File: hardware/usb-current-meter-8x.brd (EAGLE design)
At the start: 78.5 x 29.2 mm, 39 parts, among them IC3 MEGA48/88/168-AU, IC9 OPA2234U, X7 MC2

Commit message: hardware: progress save
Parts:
- added C14, C17, C19, C22, C27, C29, C4, C7: 100n, rcl:C0805
- added C15, C16, C18, C20, C21, C23, C25, C26, C28, C5, C6, C8: 1u, rcl:C0805
- added D1, D2, D3, D4: BAT54, diode:SOT23
- added IC2, IC4, IC5, IC6: OPA2234U, burr-brown:SO08
- added R10, R14, R15, R16, R17, R18, R19, R22, R23, R24, R25, R26, R27, R30, R31, R32, R33, R42, R43, R5, R6, R7, R8, R9: tbd, rcl:R0603
- added R11, R20, R28, R36: 100k, rcl:R0603
- added R12, R21, R29, R37, R4: Rload, rcl:R0805
- added X1, X2, X3, X4, X5: MC2, con-phoenix-381_l:MC2
- moved D7 11.0 mm to (45.5, 18.7)
- moved R56 11.0 mm to (37.4, 24.4)
- moved R57 11.0 mm to (37.4, 21.1)
- moved R60 11.0 mm to (37.4, 17.9)
- moved C39 11.0 mm to (38.2, 27.2)
- moved C42 11.0 mm to (43.1, 16.3)
- moved IC9 11.0 mm to (43.1, 19.9)
- moved R53 11.0 mm to (43.1, 26.4)
- moved R54 11.0 mm to (46.7, 26.4)
- moved R55 11.0 mm to (46.7, 21.5)
- moved R58 11.0 mm to (42.3, 21.1)
- moved R59 11.0 mm to (38.2, 25.6)
- moved X7 11.0 mm to (43.1, 24.0)
- moved C40 11.0 mm to (38.6, 20.3)
- moved C41 11.0 mm to (38.6, 22.4)
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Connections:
- net SC_IN_B renamed SC_IN_B_0
- removed net SC_IN_A: R53.2, R54.1, X7.1
- new net N$10: IC2.6, R7.2, R8.1
- new net N$11: IC2.7, R11.1, R8.2
- new net N$12: IC4.2, R14.2, R15.1
- new net N$13: D2.1, IC4.1
- new net N$14: D2.3, IC4.5, R15.2
- new net N$15: IC4.6, R16.2, R17.1
- new net N$16: IC4.7, R17.2, R20.1
- new net N$17: IC6.2, R30.2, R31.1
- new net N$18: D4.1, IC6.1
- new net N$19: D4.3, IC6.5, R31.2
- new net N$20: IC6.6, R32.2, R33.1
- new net N$21: IC6.7, R33.2, R36.1
- new net N$22: IC5.2, R22.2, R23.1
- new net N$23: D3.1, IC5.1
- new net N$24: D3.3, IC5.5, R23.2
- new net N$25: IC5.6, R24.2, R25.1
- new net N$26: IC5.7, R25.2, R28.1
- new net N$7: IC2.2, R5.2, R6.1
- new net N$8: D1.1, IC2.1
- new net N$9: D1.3, IC2.5, R6.2
- new net SC_IN_A_0: R29.2, R30.1, R53.2, R54.1, X4.1, X7.1
- new net SC_IN_A_1: R4.2, R5.1, X1.1
- new net SC_IN_A_2: R12.2, R14.1, X2.1
- new net SC_IN_A_3: R21.2, R22.1, X3.1
- new net SC_IN_B_1: C4.1, R10.2, R4.1, R9.1, X1.2
- new net SC_IN_B_2: C14.1, R12.1, R18.1, R19.2, X2.2
- new net SC_IN_B_3: C19.1, R21.1, R26.1, R27.2, X3.2
- new net SC_IN_B_5: C29.1, R37.1, R42.1, R43.2, X5.2
- net GND: now also C14.2, C15.2, C16.2, C17.2, C18.2, C19.2, C20.2, C21.2, C22.2, C23.2, C25.2, C26.2, C27.2, C28.2, C29.2, C4.2, C5.2, C6.2, C7.2, C8.2, IC2.3, IC2.4, IC4.3, IC4.4, IC5.3, IC5.4, IC6.3, IC6.4, R10.1, R16.1, R19.1, R24.1, R27.1, R29.1, R32.1, R43.1, R7.1, X4.2
- net IN_CH0: now also C25.1, C26.1, C28.1, R36.2
- net IN_CH1: now also C5.1, C6.1, C8.1, R11.2, R37.2, X5.1
- net IN_CH2: now also C15.1, C16.1, C18.1, R20.2
- net IN_CH3: now also C20.1, C21.1, C23.1, R28.2
- net VCC: now also C17.1, C22.1, C27.1, C7.1, IC2.8, IC4.8, IC5.8, IC6.8, R18.2, R26.2, R42.2, R9.2
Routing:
- net VCC: track 64.1 -> 85.3 mm, vias 5 -> 7
- net IN_CH1: track 0.00 -> 10.7 mm, vias 0 -> 1
- net SC_IN_B_2: track 0.00 -> 10.3 mm
- net SC_IN_B_1: track 0.00 -> 10.3 mm
- net SC_IN_B_3: track 0.00 -> 10.3 mm
- net N$7: track 0.00 -> 9.73 mm, vias 0 -> 1
- net N$12: track 0.00 -> 9.73 mm, vias 0 -> 1
- net N$22: track 0.00 -> 9.73 mm, vias 0 -> 1
- net SC_IN_B_5: track 0.00 -> 8.94 mm
- net N$14: track 0.00 -> 8.79 mm, vias 0 -> 1
- net N$24: track 0.00 -> 8.79 mm, vias 0 -> 1
- net IN_CH3: track 0.00 -> 7.69 mm, vias 0 -> 1
- net IN_CH2: track 0.00 -> 7.69 mm, vias 0 -> 1
- net N$9: track 0.00 -> 6.74 mm, vias 0 -> 1
- net SC_IN_A_0: track 0.00 -> 5.89 mm
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
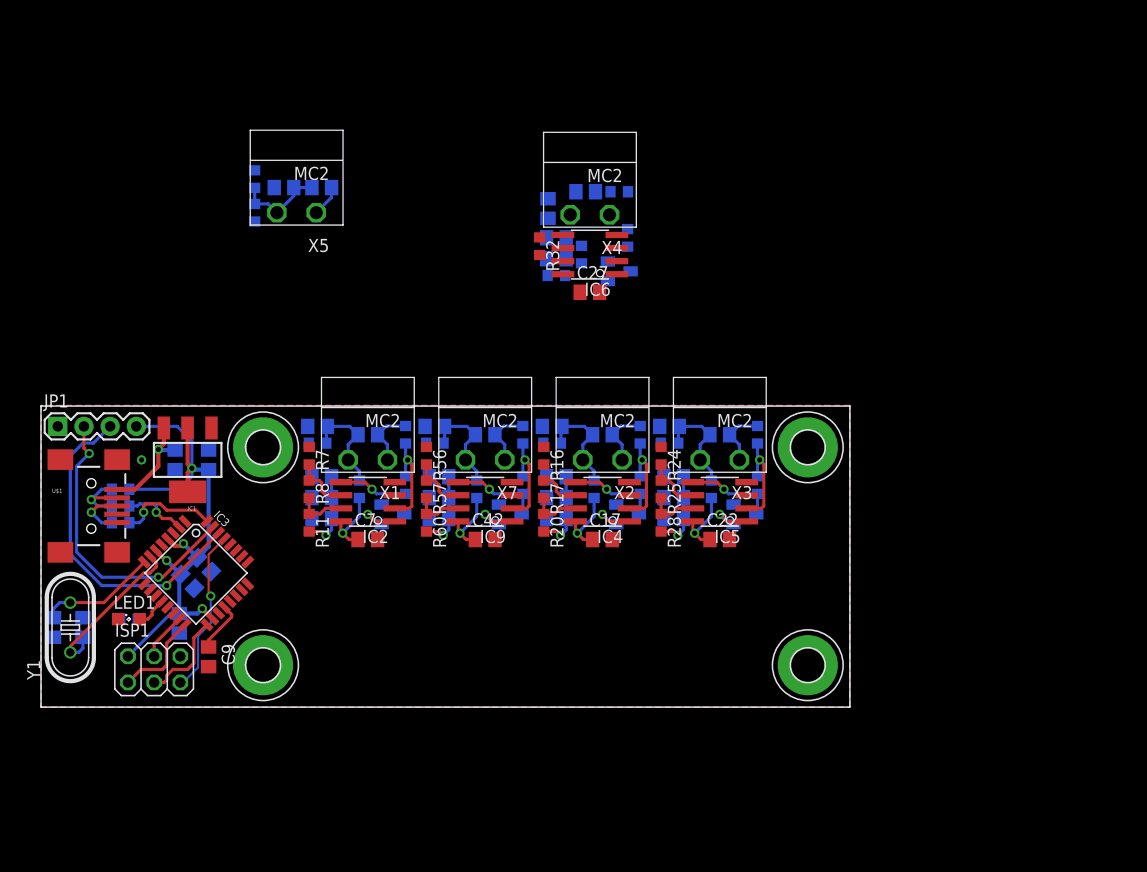
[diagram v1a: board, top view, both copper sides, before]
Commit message: hardware: 8x schematic updated
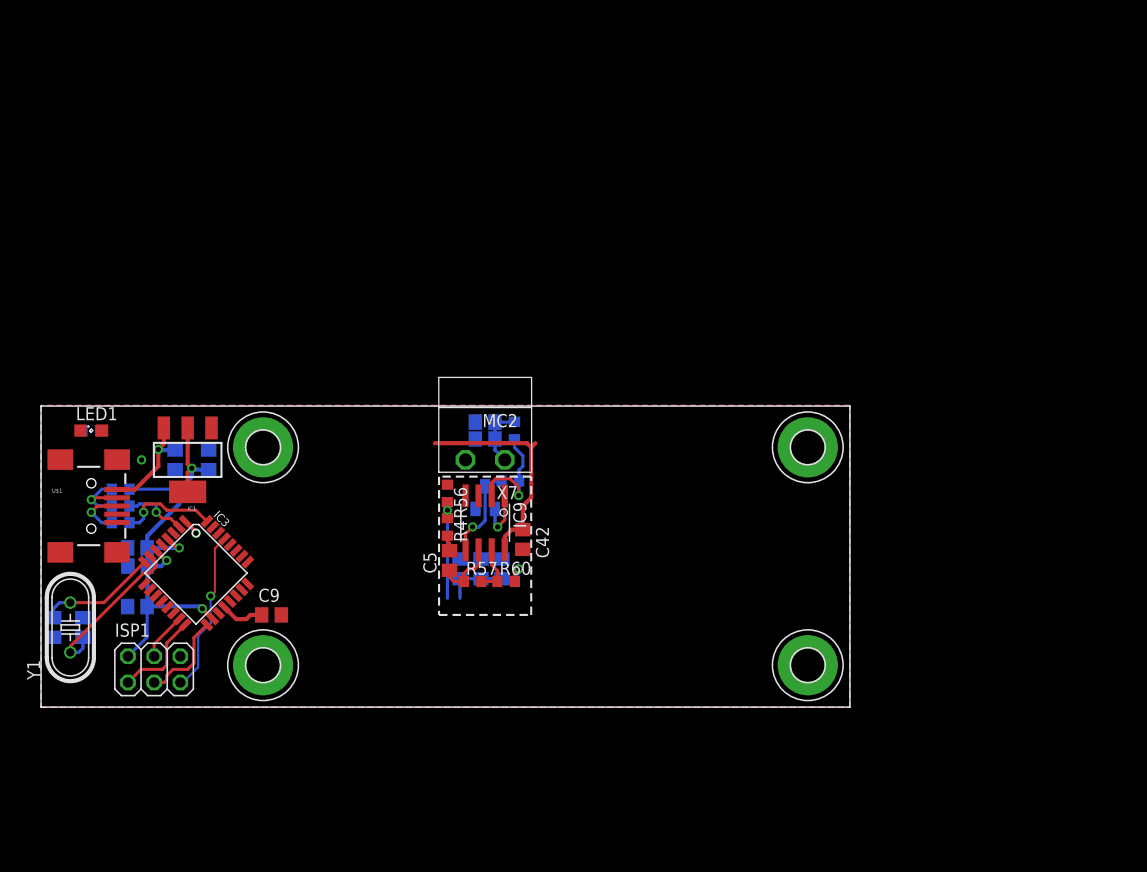
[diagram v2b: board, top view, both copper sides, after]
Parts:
- removed C14, C17, C19, C22, C27, C29, C39, C7: 100n, rcl:C0805
- removed C15, C16, C18, C20, C21, C23, C25, C26, C28, C6, C8: 1u, rcl:C0805
- removed D1, D2, D3, D4: BAT54, diode:SOT23
- removed IC2, IC4, IC5, IC6: OPA2234U, burr-brown:SO08
- removed JP1: (no value), SparkFun:1X04
- removed R10, R14, R15, R16, R17, R18, R19, R22, R23, R24, R25, R26, R27, R30, R31, R32, R33, R42, R43, R5, R58, R59, R6, R7, R8, R9: tbd, rcl:R0603
- removed R11, R20, R28, R36: 100k, rcl:R0603
- removed R12, R21, R29, R37: Rload, rcl:R0805
- removed X1, X2, X3, X4, X5: MC2, con-phoenix-381_l:MC2
- C5: value 1u -> 100n
- R4: value Rload -> tbd; device rcl:R0805 -> rcl:R0603
- moved LED1 18.7 mm to (4.88, 26.8)
- moved R13 18.7 mm to (4.88, 26.8)
- moved C4 16.3 mm to (43.1, 27.6)
- moved C5 13.0 mm to (39.6, 14.2), flipped to the top, turned to 90 degrees
- moved R4 11.8 mm to (39.4, 17.5), flipped to the top, turned to 270 degrees
- moved R57 10.00 mm to (41.9, 12.2), turned to 0 degrees
- moved R60 9.59 mm to (45.1, 12.2), turned to 0 degrees
- moved C41 9.17 mm to (40.6, 13.4), turned to 90 degrees
- moved C40 8.02 mm to (42.7, 13.4), turned to 90 degrees
- moved C43 7.81 mm to (44.7, 13.4), turned to 90 degrees
- moved C9 7.33 mm to (22.4, 8.94), turned to 0 degrees
- moved C13 6.70 mm to (9.35, 15.4), turned to 0 degrees
- moved C3 5.07 mm to (9.37, 13.7), turned to 0 degrees
- moved C12 4.38 mm to (9.35, 9.75), turned to 0 degrees
- moved R56 4.18 mm to (39.4, 20.7)
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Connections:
- net IN_CH4 renamed CH4
- net IN_CH5 renamed CH5
- net IN_CH6 renamed CH6
- net IN_CH7 renamed CH7
- removed net IN_CH0: C25.1, C26.1, C28.1, C40.1, C41.1, C43.1, IC3.23, R36.2, R60.2
- removed net IN_CH1: C5.1, C6.1, C8.1, IC3.24, R11.2, R37.2, X5.1
- removed net IN_CH2: C15.1, C16.1, C18.1, IC3.25, R20.2
- removed net IN_CH3: C20.1, C21.1, C23.1, IC3.26, R28.2
- removed net N$10: IC2.6, R7.2, R8.1
- removed net N$11: IC2.7, R11.1, R8.2
- removed net N$12: IC4.2, R14.2, R15.1
- removed net N$13: D2.1, IC4.1
- removed net N$14: D2.3, IC4.5, R15.2
- removed net N$15: IC4.6, R16.2, R17.1
- removed net N$16: IC4.7, R17.2, R20.1
- removed net N$17: IC6.2, R30.2, R31.1
- removed net N$18: D4.1, IC6.1
- removed net N$19: D4.3, IC6.5, R31.2
- removed net N$20: IC6.6, R32.2, R33.1
- removed net N$21: IC6.7, R33.2, R36.1
- removed net N$22: IC5.2, R22.2, R23.1
- removed net N$23: D3.1, IC5.1
- removed net N$24: D3.3, IC5.5, R23.2
- removed net N$25: IC5.6, R24.2, R25.1
- removed net N$26: IC5.7, R25.2, R28.1
- removed net N$8: D1.1, IC2.1
- removed net N$9: D1.3, IC2.5, R6.2
- removed net SC_IN_A_0: R29.2, R30.1, R53.2, R54.1, X4.1, X7.1
- removed net SC_IN_A_1: R4.2, R5.1, X1.1
- removed net SC_IN_A_2: R12.2, R14.1, X2.1
- removed net SC_IN_A_3: R21.2, R22.1, X3.1
- removed net SC_IN_B_0: C39.1, R53.1, R58.1, R59.2, X7.2
- removed net SC_IN_B_1: C4.1, R10.2, R4.1, R9.1, X1.2
- removed net SC_IN_B_2: C14.1, R12.1, R18.1, R19.2, X2.2
- removed net SC_IN_B_3: C19.1, R21.1, R26.1, R27.2, X3.2
- removed net SC_IN_B_5: C29.1, R37.1, R42.1, R43.2, X5.2
- removed net UART_RX: IC3.30, JP1.3
- removed net UART_TX: IC3.31, JP1.2
- new net CH0: C40.1, C41.1, C43.1, IC3.23, R60.2
- new net CH0_GAIN: IC3.30, R4.1, R56.2
- new net CH0_IN: C4.1, R53.2, R54.1, X7.1
- new net CH1: IC3.24
- new net CH1_GAIN: IC3.31
- new net CH2: IC3.25
- new net CH2_GAIN: IC3.9
- new net CH3: IC3.26
- new net CH3_GAIN: IC3.10
- new net CH4_GAIN: IC3.11
- new net CH5_GAIN: IC3.12
- new net CH6_GAIN: IC3.13
- new net CH7_GAIN: IC3.14
- net GND: now also R53.1, X7.2; no longer C14.2, C15.2, C16.2, C17.2, C18.2, C19.2, C20.2, C21.2, C22.2, C23.2, C25.2, C26.2, C27.2, C28.2, C29.2, C39.2, C5.2, C6.2, C7.2, C8.2, IC2.3, IC2.4, IC4.3, IC4.4, IC5.3, IC5.4, IC6.3, IC6.4, JP1.1, R10.1, R16.1, R19.1, R24.1, R27.1, R29.1, R32.1, R43.1, R59.1, R7.1, X4.2
- net LED: now also IC3.1; no longer IC3.12
- net N$40: now also C5.1; no longer R56.2
- net N$7: now also C5.2, R4.2; no longer IC2.2, R5.2, R6.1
- net VCC: no longer C17.1, C22.1, C27.1, C7.1, IC2.8, IC4.8, IC5.8, IC6.8, JP1.4, R18.2, R26.2, R42.2, R58.2, R9.2
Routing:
- net UART_RX: track 32.4 -> 0.00 mm, vias 1 -> 0
- net UART_TX: track 29.1 -> 0.00 mm, vias 2 -> 0
- net VCC: track 85.3 -> 70.6 mm, vias 7 -> 4
- net IN_CH1: track 10.7 -> 0.00 mm, vias 1 -> 0
- net SC_IN_B_2: track 10.3 -> 0.00 mm
- net SC_IN_B_0: track 10.3 -> 0.00 mm
- net SC_IN_B_1: track 10.3 -> 0.00 mm
- net SC_IN_B_3: track 10.3 -> 0.00 mm
- net CH0_GAIN: track 0.00 -> 10.1 mm, vias 0 -> 1
- net N$12: track 9.73 -> 0.00 mm, vias 1 -> 0
- net N$22: track 9.73 -> 0.00 mm, vias 1 -> 0
- net CH0: track 0.00 -> 9.59 mm, vias 0 -> 1
- net SC_IN_B_5: track 8.94 -> 0.00 mm
- net N$14: track 8.79 -> 0.00 mm, vias 1 -> 0
- net N$24: track 8.79 -> 0.00 mm, vias 1 -> 0
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
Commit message: 8x: progress save
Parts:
- added JP1: (no value), SparkFun-Connectors:1X04
- added U$2: Fabio Baltieri, balto:CREATIVE_COMMONS
- moved R57 0.81 mm to (41.9, 13.0)
- moved R60 0.81 mm to (45.1, 13.0)
- moved R4 0.41 mm to (39.8, 17.5)
- moved R56 0.41 mm to (39.8, 20.7)
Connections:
- new net RX: JP1.3
- new net TX: JP1.2
- net GND: now also JP1.1
- net VCC: now also JP1.4
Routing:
- net N$4: track 15.8 -> 5.17 mm
- net N$5: track 11.5 -> 2.75 mm
- net N$40: track 6.25 -> 4.35 mm
- net N$41: track 4.85 -> 3.71 mm
- net VCC: track 70.6 -> 69.5 mm

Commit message: 8x: progress save
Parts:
- added C14, C17, C18, C20, C23, C24, C26, C29, C30, C32, C35, C36, C38, C45, C46, C48, C51, C52, C54, C6, C7: 1u, rcl:C0805
- added C15, C19, C21, C25, C27, C31, C33, C37, C39, C47, C49, C53, C55, C8: 100n, rcl:C0805
- added C16, C22, C28, C34, C44, C50, C56: 0, rcl:C0805
- added C57: .1u, rcl:C0805
- added D1, D2, D3, D4, D5, D6, D8: BAT54, diode:SOT23
- added IC10, IC2, IC4, IC5, IC6, IC7, IC8: OPA2234U, burr-brown:SO08
- added IC12: LTC485S, linear-technology:SOIC8
- added JP2: (no value), SparkFun-Connectors:1X02
- added R10, R18, R25, R32, R39, R46, R58: 100k, rcl:R0603
- added R11, R19, R26, R33, R40, R47, R59: Rh, rcl:R0603
- added R12, R20, R27, R34, R41, R48, R5: Rload, rcl:R0805
- added R14, R15, R21, R22, R28, R29, R35, R36, R42, R43, R49, R50, R6, R7: 10k, rcl:R0603
- added R16, R23, R30, R37, R44, R51, R8: Rl, rcl:R0603
- added R17, R24, R31, R38, R45, R52, R9: Rx, rcl:R0603
- added R61: 120, rcl:R0603
- added U3: RJ45-8PTH, SparkFun-Connectors:RJ45-8
- added X1, X2, X3, X4, X5, X6, X8: MC2, con-phoenix-381_l:MC2
- C12, C13, C3, C9: value 100n -> .1u
- C5: value 100n -> 0
- R4: value tbd -> Rh
- R54, R55: value tbd -> 10k
- R56: value tbd -> Rl
- R57: value tbd -> Rx
- moved JP1 66.3 mm to (57.5, 21.1), turned to 270 degrees
- moved ISP1 62.6 mm to (64.8, 35.6), turned to 180 degrees
- moved C10 50.5 mm to (51.6, 4.47), turned to 180 degrees
- moved C12 49.8 mm to (55.3, 29.1), turned to 270 degrees
- moved Y1 48.8 mm to (51.6, 6.10), turned to 180 degrees
- moved C11 47.6 mm to (51.6, 7.32), turned to 0 degrees
- moved C9 47.4 mm to (57.1, 41.2), turned to 90 degrees
- moved C3 44.7 mm to (51.4, 29.1), turned to 270 degrees
- moved IC3 42.9 mm to (52.0, 34.7), turned to 45 degrees
- moved C4 42.8 mm to (17.9, 62.2)
- moved C41 42.8 mm to (15.4, 48.0)
- moved C43 42.8 mm to (19.5, 48.0)
- moved C5 42.8 mm to (14.4, 48.8)
- moved D7 42.8 mm to (17.9, 54.9)
- moved IC9 42.8 mm to (17.9, 52.4)
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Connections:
- removed net MISO: IC3.16, ISP1.1
- removed net MOSI: IC3.15, ISP1.4
- removed net RX: JP1.3
- removed net SCK: IC3.17, ISP1.3
- removed net TX: JP1.2
- new net 485_N: IC12.7, R61.1, U3.2
- new net 485_P: IC12.6, R61.2, U3.1
- new net CH0_IN1: C15.1, R5.2, R6.1, X1.1
- new net CH0_IN2: C21.1, R12.2, R14.1, X2.1
- new net CH0_IN3: C33.1, R27.2, R28.1, X4.1
- new net CH0_IN4: C39.1, R34.2, R35.1, X5.1
- new net CH0_IN5: C55.1, R48.2, R49.1, X8.1
- new net CH0_IN6: C27.1, R20.2, R21.1, X3.1
- new net CH0_IN8: C49.1, R41.2, R42.1, X6.1
- new net N$10: D1.3, IC2.5, R7.2
- new net N$11: C16.1, IC2.6, R9.1
- new net N$12: IC2.7, R10.1, R9.2
- new net N$13: C16.2, R11.2
- new net N$14: IC4.2, R14.2, R15.1
- new net N$15: D2.1, IC4.1
- new net N$16: D2.3, IC4.5, R15.2
- new net N$17: C22.1, IC4.6, R17.1
- new net N$18: IC4.7, R17.2, R18.1
- new net N$19: C22.2, R19.2
- new net N$20: IC6.2, R28.2, R29.1
- new net N$21: D4.1, IC6.1
- new net N$22: D4.3, IC6.5, R29.2
- new net N$23: C34.1, IC6.6, R31.1
- new net N$24: IC6.7, R31.2, R32.1
- new net N$25: C34.2, R33.2
- new net N$26: IC7.2, R35.2, R36.1
- new net N$27: D5.1, IC7.1
- new net N$28: D5.3, IC7.5, R36.2
- new net N$29: C44.1, IC7.6, R38.1
- new net N$30: IC7.7, R38.2, R39.1
- new net N$31: C44.2, R40.2
- new net N$32: IC10.2, R49.2, R50.1
- new net N$33: D8.1, IC10.1
- new net N$34: D8.3, IC10.5, R50.2
- new net N$35: C56.1, IC10.6, R52.1
- new net N$36: IC10.7, R52.2, R58.1
- new net N$42: C56.2, R59.2
- new net N$43: IC5.2, R21.2, R22.1
- new net N$44: D3.1, IC5.1
- new net N$45: D3.3, IC5.5, R22.2
- new net N$46: C28.1, IC5.6, R24.1
- new net N$47: IC5.7, R24.2, R25.1
- new net N$48: C28.2, R26.2
- new net N$49: IC12.1, JP2.2
- new net N$55: IC8.2, R42.2, R43.1
- new net N$56: D6.1, IC8.1
- new net N$57: D6.3, IC8.5, R43.2
- new net N$58: C50.1, IC8.6, R45.1
- new net N$59: IC8.7, R45.2, R46.1
- new net N$60: C50.2, R47.2
- new net N$8: IC2.2, R6.2, R7.1
- new net N$9: D1.1, IC2.1
- new net UART_EN: IC12.2, IC12.3, IC3.1, ISP1.3
- new net UART_RX: IC3.30, JP1.3, JP2.1
- new net UART_TX: IC12.4, IC3.31, JP1.2
- net +5V: now also U3.4, U3.5
- net CH0: now also IC3.28; no longer IC3.23
- net CH0_GAIN: now also IC3.16, ISP1.1; no longer IC3.30
- net CH1: now also C14.1, C6.1, C7.1, IC3.27, R10.2; no longer IC3.24
- net CH1_GAIN: now also IC3.17, ISP1.4, R11.1, R8.2; no longer IC3.31
- net CH2: now also C17.1, C18.1, C20.1, IC3.26, R18.2; no longer IC3.25
- net CH2_GAIN: now also R16.2, R19.1
- net CH3: now also C23.1, C24.1, C26.1, IC3.25, R25.2; no longer IC3.26
- net CH3_GAIN: now also R23.2, R26.1
- net CH4: now also C29.1, C30.1, C32.1, IC3.24, R32.2; no longer IC3.27
- net CH4_GAIN: now also R30.2, R33.1
- net CH5: now also C35.1, C36.1, C38.1, IC3.23, R39.2; no longer IC3.28
- net CH5_GAIN: now also R37.2, R40.1
- net CH6: now also C45.1, C46.1, C48.1, IC3.22, R46.2; no longer IC3.19
- net CH6_GAIN: now also R44.2, R47.1
- net CH7: now also C51.1, C52.1, C54.1, IC3.19, R58.2; no longer IC3.22
- net CH7_GAIN: now also R51.2, R59.1
- net GND: now also C14.2, C15.2, C17.2, C18.2, C19.2, C20.2, C21.2, C23.2, C24.2, C25.2, C26.2, C27.2, C29.2, C30.2, C31.2, C32.2, C33.2, C35.2, C36.2, C37.2, C38.2, C39.2, C45.2, C46.2, C47.2, C48.2, C49.2, C51.2, C52.2, C53.2, C54.2, C55.2, C57.2, C6.2, C7.2, C8.2, IC10.3, IC10.4, IC12.5, IC2.3, IC2.4, IC4.3, IC4.4, IC5.3, IC5.4, IC6.3, IC6.4, IC7.3, IC7.4, IC8.3, IC8.4, R12.1, R16.1, R20.1, R23.1, R27.1, R30.1, R34.1, R37.1, R41.1, R44.1, R48.1, R5.1, R51.1, R8.1, U3.7, U3.8, X1.2, X2.2, X3.2, X4.2, X5.2, X6.2, X8.2
- net LED: now also IC3.15; no longer IC3.1
- net VCC: now also C19.1, C25.1, C31.1, C37.1, C47.1, C53.1, C57.1, C8.1, IC10.8, IC12.8, IC2.8, IC4.8, IC5.8, IC6.8, IC7.8, IC8.8
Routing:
- net VCC: track 69.5 -> 203.0 mm
- net CH7: track 0.00 -> 42.1 mm, vias 0 -> 2
- net CH1: track 0.00 -> 38.5 mm, vias 0 -> 2
- net CH0: track 9.40 -> 47.8 mm, vias 1 -> 2
- net CH6: track 0.00 -> 33.6 mm, vias 0 -> 2
- net CH2: track 0.00 -> 29.1 mm, vias 0 -> 2
- net CH5: track 0.00 -> 24.2 mm, vias 0 -> 2
- net CH3: track 0.00 -> 19.7 mm, vias 0 -> 2
- net CH4_GAIN: track 0.00 -> 19.1 mm, vias 0 -> 2
- net CH4: track 0.00 -> 15.3 mm, vias 0 -> 2
- net CH1_GAIN: track 0.00 -> 14.9 mm, vias 0 -> 2
- net CH7_GAIN: track 0.00 -> 13.3 mm, vias 0 -> 2
- net CH6_GAIN: track 0.00 -> 13.3 mm, vias 0 -> 2
- net CH5_GAIN: track 0.00 -> 13.3 mm, vias 0 -> 2
- net CH3_GAIN: track 0.00 -> 13.3 mm, vias 0 -> 2
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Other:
- board size 78.5 x 29.2 mm -> 105.3 x 64.2 mm

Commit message: 8x: progress save
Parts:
- removed H1, H2, H3, H4: MOUNT-PAD-ROUND3.2, holes:3,2-PAD
- added BOX1: HAMMOND-BOX-XXA, hammond:1591XXA
- moved C2 79.3 mm to (89.0, 13.0), turned to 90 degrees
- moved IC1 78.2 mm to (87.8, 13.0), turned to 0 degrees
- moved C1 76.6 mm to (85.8, 13.0), turned to 270 degrees
- moved U3 63.6 mm to (25.0, 3.25), turned to 0 degrees
- moved LED1 57.7 mm to (92.0, 20.9), turned to 270 degrees
- moved R13 57.7 mm to (92.0, 20.9), turned to 90 degrees
- moved R2 39.6 mm to (66.6, 7.72)
- moved U$1 39.6 mm to (66.6, 4.88)
- moved R1 39.6 mm to (68.3, 7.72)
- moved R3 39.6 mm to (65.0, 7.72)
- moved C57 36.3 mm to (34.1, 9.55), turned to 270 degrees
- moved IC12 29.4 mm to (37.8, 9.55), turned to 0 degrees
- moved JP2 28.3 mm to (39.0, 3.45), turned to 180 degrees
- moved R61 27.6 mm to (37.8, 14.8), turned to 0 degrees
- moved IC10 26.1 mm to (81.3, 26.8)
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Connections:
- net GND: no longer H1.B3,2, H2.B3,2, H3.B3,2, H4.B3,2
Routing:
- net +5V: track 7.32 -> 69.3 mm
- net CH0: track 47.8 -> 55.2 mm
- net N$37: track 11.4 -> 17.9 mm
- net N$32: track 11.4 -> 17.9 mm
- net CH3: track 19.7 -> 25.6 mm
- net CH2: track 29.1 -> 35.0 mm
- net CH1: track 38.5 -> 44.4 mm
- net CH6: track 33.6 -> 27.7 mm
- net CH4_GAIN: track 19.1 -> 24.6 mm
- net CH7: track 42.1 -> 37.4 mm
- net CH7_GAIN: track 13.3 -> 10.2 mm
- net CH5_GAIN: track 13.3 -> 16.2 mm
- net CH0_GAIN: track 20.2 -> 17.8 mm
- net CH5: track 24.2 -> 22.4 mm
- net VCC: track 203.0 -> 202.2 mm
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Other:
- board size 105.3 x 64.2 mm -> 94 x 44.5 mm

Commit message: 8x: progress save
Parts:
- removed JP2: (no value), SparkFun-Connectors:1X02
- added D9: BAT54C, diode:SOT23
- moved LED1 33.7 mm to (60.6, 8.94), turned to 180 degrees
- moved R13 31.2 mm to (62.6, 10.6), flipped to the top, turned to 180 degrees
- moved R1 7.89 mm to (61.8, 3.25), flipped to the top, turned to 180 degrees
- moved C2 5.93 mm to (85.3, 8.33), flipped to the top, turned to 0 degrees
- moved R2 5.65 mm to (61.8, 4.88), flipped to the top, turned to 180 degrees
- moved C1 5.47 mm to (87.8, 18.1), flipped to the top, turned to 180 degrees
- moved U3 4.98 mm to (26.0, 8.13)
- moved R3 3.47 mm to (61.8, 6.50), flipped to the top, turned to 180 degrees
- moved ISP1 3.45 mm to (69.7, 15.0), turned to 180 degrees
- moved U$1 3.35 mm to (69.9, 5.69)
- moved IC12 3.05 mm to (40.2, 11.4)
- moved R61 3.05 mm to (40.2, 16.7)
- moved C57 2.32 mm to (35.6, 11.4)
- moved JP1 1.24 mm to (43.9, 3.66), turned to 180 degrees
- moved IC1 0.57 mm to (87.4, 13.4), turned to 270 degrees
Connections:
- removed net N$49: IC12.1, JP2.2
- new net VIN_BUS: D9.1, U3.4, U3.5
- new net VIN_USB: D9.2, U$1.VBUS
- net +5V: now also D9.3; no longer U$1.VBUS, U3.4, U3.5
- net CH0_GAIN: now also IC3.9; no longer IC3.16, ISP1.1
- net CH1_GAIN: now also IC3.10; no longer IC3.17, ISP1.4
- net CH2_GAIN: now also IC3.11; no longer IC3.9
- net CH3_GAIN: now also IC3.12; no longer IC3.10
- net CH4_GAIN: now also IC3.17, ISP1.3; no longer IC3.11
- net CH5_GAIN: now also IC3.16, ISP1.1; no longer IC3.12
- net CH6_GAIN: now also IC3.14; no longer IC3.13
- net CH7_GAIN: now also IC3.13; no longer IC3.14
- net LED: now also ISP1.4
- net UART_EN: no longer ISP1.3
- net UART_RX: now also IC12.1; no longer JP2.1
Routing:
- net VCC: track 202.2 -> 284.8 mm, vias 4 -> 6
- net VIN_BUS: track 0.00 -> 67.0 mm
- net +5V: track 69.3 -> 13.5 mm
- net CH0_GAIN: track 17.8 -> 62.2 mm, vias 2 -> 4
- net CH1_GAIN: track 15.6 -> 54.3 mm, vias 2 -> 4
- net CH2_GAIN: track 13.3 -> 46.4 mm, vias 2 -> 4
- net 485_P: track 0.00 -> 28.4 mm
- net UART_RX: track 0.00 -> 23.9 mm
- net CH3_GAIN: track 13.3 -> 36.9 mm, vias 2 -> 4
- net USB_DP: track 5.73 -> 29.2 mm, vias 1 -> 0
- net CH5_GAIN: track 16.2 -> 38.9 mm, vias 2 -> 3
- net CH7_GAIN: track 10.2 -> 32.7 mm
- net 485_N: track 0.00 -> 21.9 mm
- net USB_DN: track 5.04 -> 26.4 mm, vias 1 -> 0
- net LED: track 0.00 -> 20.3 mm, vias 0 -> 3
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- added copper zone on layer 1, net VCC
